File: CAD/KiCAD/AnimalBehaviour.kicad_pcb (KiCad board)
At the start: 2 copper layers, 29 parts, among them J1 Conn_01x06_Male, J10 Conn_01x02_Male, J11 Conn_01x03_Male, J12 Conn_01x02_Male, J2 Conn_01x02_Male, J3 Conn_01x04_Male, J4 Conn_01x08_Male, J5 Conn_01x02_Male, J6 Conn_01x02_Male, J7 Jack-DC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

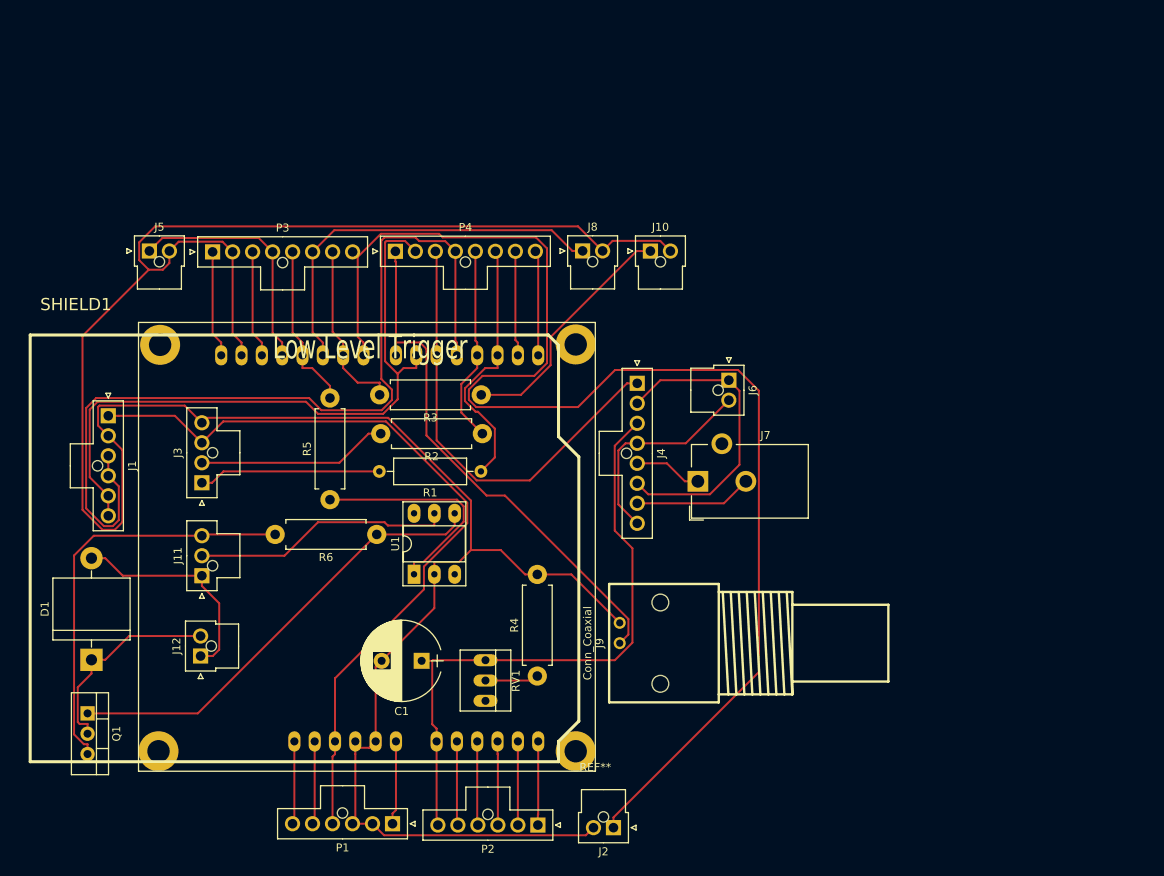
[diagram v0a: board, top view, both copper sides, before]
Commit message: Added new schematics, aduino footprints etc.
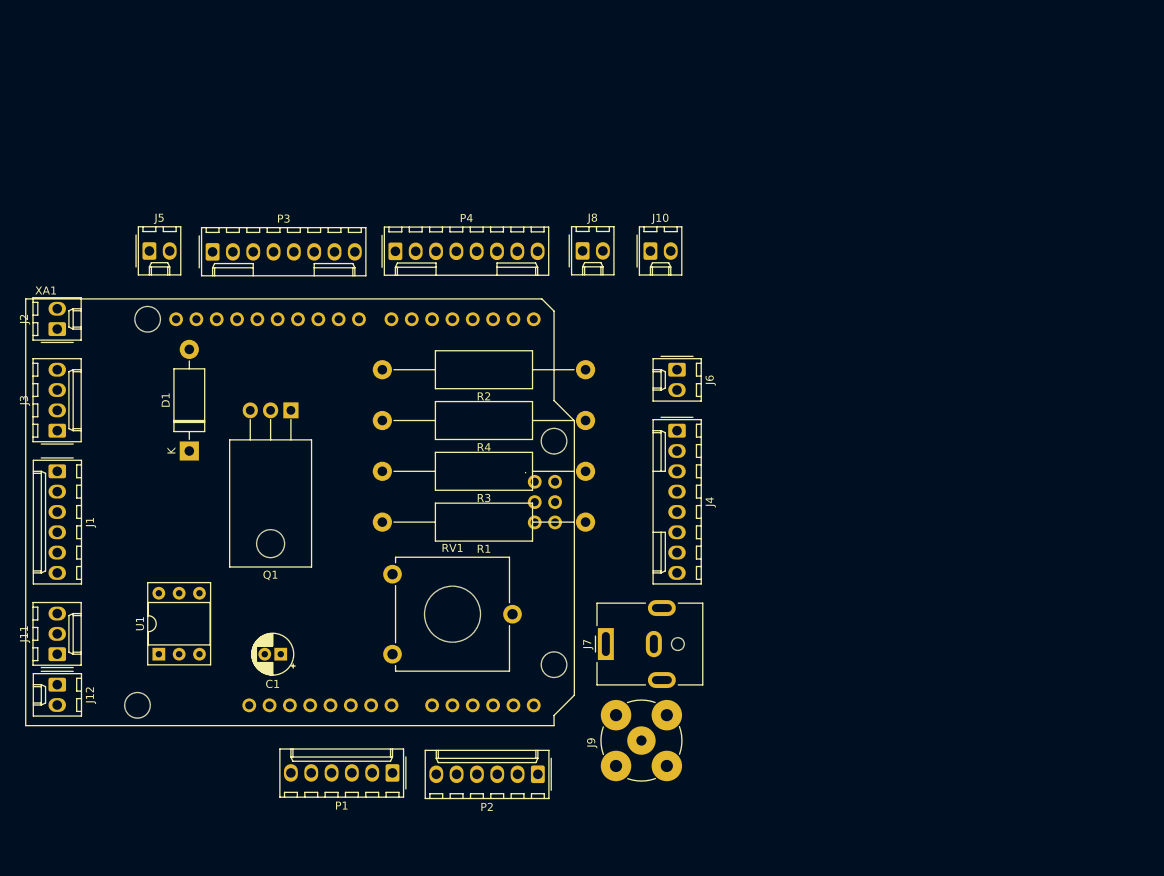
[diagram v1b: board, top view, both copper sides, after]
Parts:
- removed R5: 470E, Resistors_ThroughHole:R_Axial_DIN0411_L9.9mm_D3.6mm_P12.70mm_Horizontal
- removed R6: 10K, Resistors_ThroughHole:R_Axial_DIN0411_L9.9mm_D3.6mm_P12.70mm_Horizontal
- removed REF**: 4ChannelSSR, 4ChannelSSR
- removed SHIELD1: ARDUINO_SHIELD, arduino_shields:ARDUINO_SHIELD_040pins
- added XA1: Arduino_Uno_Shield, Arduino:Arduino_Uno_Shield, F.Cu at (86.2, 125.8)
- C1: footprint Capacitors_ThroughHole:CP_Radial_D10.0mm_P5.00mm -> Capacitor_THT:CP_Radial_D5.0mm_P2.00mm
- D1: footprint Diodes_ThroughHole:D_5KP_P12.70mm_Horizontal -> Diode_THT:D_DO-15_P12.70mm_Horizontal
- J1, P1, P2: footprint Connectors_Molex:Molex_NanoFit_1x06x2.50mm_Straight -> Connector_Molex:Molex_KK-254_AE-6410-06A_1x06_P2.54mm_Vertical
- J10, J12, J2, J5, J6, J8: footprint Connectors_Molex:Molex_NanoFit_1x02x2.50mm_Straight -> Connector_Molex:Molex_KK-254_AE-6410-02A_1x02_P2.54mm_Vertical
- J11: footprint Connectors_Molex:Molex_NanoFit_1x03x2.50mm_Straight -> Connector_Molex:Molex_KK-254_AE-6410-03A_1x03_P2.54mm_Vertical
- J3: footprint Connectors_Molex:Molex_NanoFit_1x04x2.50mm_Straight -> Connector_Molex:Molex_KK-254_AE-6410-04A_1x04_P2.54mm_Vertical
- J4, P3, P4: footprint Connectors_Molex:Molex_NanoFit_1x08x2.50mm_Straight -> Connector_Molex:Molex_KK-254_AE-6410-08A_1x08_P2.54mm_Vertical
- J7: footprint Connect:Barrel_Jack_CUI_PJ-102AH -> Connector_BarrelJack:BarrelJack_CUI_PJ-063AH_Horizontal
- J9: footprint w_conn_rf:bnc_90_1-1337543-0 -> Connector_Coaxial:BNC_TEConnectivity_1478204_Vertical
- Q1: footprint TO_SOT_Packages_THT:TO-220-3_Vertical -> Package_TO_SOT_THT:TO-220-3_Horizontal_TabDown
- R1: value 560E -> 470E; footprint Resistors_ThroughHole:R_Axial_DIN0309_L9.0mm_D3.2mm_P12.70mm_Horizontal -> Resistor_THT:R_Axial_DIN0414_L11.9mm_D4.5mm_P25.40mm_Horizontal
- R2: value 560E -> 1K; footprint Resistors_ThroughHole:R_Axial_DIN0411_L9.9mm_D3.6mm_P12.70mm_Horizontal -> Resistor_THT:R_Axial_DIN0414_L11.9mm_D4.5mm_P25.40mm_Horizontal
- R3: footprint Resistors_ThroughHole:R_Axial_DIN0411_L9.9mm_D3.6mm_P12.70mm_Horizontal -> Resistor_THT:R_Axial_DIN0414_L11.9mm_D4.5mm_P25.40mm_Horizontal
- R4: value 1K -> 10K; footprint Resistors_ThroughHole:R_Axial_DIN0411_L9.9mm_D3.6mm_P12.70mm_Horizontal -> Resistor_THT:R_Axial_DIN0414_L11.9mm_D4.5mm_P25.40mm_Horizontal
- RV1: footprint Connect:PINHEAD1-3 -> Potentiometer_THT:Potentiometer_ACP_CA14V-15_Vertical_Hole
- U1: footprint Housings_DIP:DIP-6_W7.62mm_Socket_LongPads -> Package_DIP:DIP-6_W7.62mm_Socket
- moved J2 93.4 mm to (90.2, 76.2), turned to 90 degrees
- moved Q1 45.6 mm to (119.4, 86.4), turned to 180 degrees
- moved U1 33.4 mm to (102.9, 116.8)
- moved R4 32.5 mm to (156.2, 87.6), turned to 180 degrees
- moved D1 28.8 mm to (106.7, 91.4)
- moved J7 23.4 mm to (158.8, 115.6)
- moved J11 20.6 mm to (90.2, 116.8)
- moved J3 19.2 mm to (90.2, 88.9)
- moved J12 18.3 mm to (90.2, 120.7), turned to 270 degrees
- moved C1 17.6 mm to (118.1, 116.8)
- moved R3 16.2 mm to (156.2, 94.0)
- moved J9 15.5 mm to (163.2, 127.6)
- moved R2 15.2 mm to (156.2, 81.3)
- moved R1 14.5 mm to (156.2, 100.3)
- moved RV1 11.6 mm to (132.1, 116.8), turned to 0 degrees
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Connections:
- J3 pad 1: Net-(J3-Pad1) -> D2
- J3 pad 2: Net-(J3-Pad2) -> D3
- P4 pad 7: D1 -> (no net)
- P4 pad 8: D0 -> (no net)
- R1 pad 1: D2 -> Net-(J10-Pad1)
- R1 pad 2: Net-(J3-Pad1) -> D9
- R2 pad 1: D3 -> Net-(R2-Pad1)
- R2 pad 2: Net-(J3-Pad2) -> DGND
- R3 pad 1: Net-(J10-Pad1) -> Net-(R3-Pad1)
- R3 pad 2: D9 -> D11
- R4 pad 1: Net-(R4-Pad1) -> Net-(Q1-Pad1)
- R4 pad 2: DGND -> AGND
- RV1 pad 2: Net-(R4-Pad1) -> Net-(R2-Pad1)
- RV1 pad 3: Net-(RV1-Pad3) -> (no net)
- U1 pad 1: Net-(R5-Pad1) -> Net-(R3-Pad1)
- U1 pad 3: Net-(U1-Pad3) -> (no net)
- U1 pad 6: Net-(U1-Pad6) -> (no net)
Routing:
- net DGND: track 311.3 -> 0.00 mm
- net D8: track 167.6 -> 0.00 mm
- net D4: track 110.0 -> 0.00 mm
- net 5V: track 98.7 -> 0.00 mm
- net D6: track 83.4 -> 0.00 mm
- net A0: track 77.6 -> 0.00 mm
- net D7: track 66.2 -> 0.00 mm
- net Net-(Q1-Pad1): track 57.1 -> 0.00 mm
- net D5: track 55.9 -> 0.00 mm
- net AGND: track 52.0 -> 0.00 mm
- net D10: track 49.4 -> 0.00 mm
- net PAD+: track 38.6 -> 0.00 mm
- net D2: track 32.7 -> 0.00 mm
- net EX_5V: track 32.5 -> 0.00 mm
- net Net-(J10-Pad1): track 30.7 -> 0.00 mm
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
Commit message: v2019.07.06.alpha1
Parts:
- removed the J2 at (90.2, 76.2)
- removed the J8 at (155.8, 66.4)
- removed P1, P2: CONN_6, Connector_Molex:Molex_KK-254_AE-6410-06A_1x06_P2.54mm_Vertical
- removed P3, P4: CONN_8, Connector_Molex:Molex_KK-254_AE-6410-08A_1x08_P2.54mm_Vertical
- removed the R2 at (156.2, 81.3)
- removed the R4 at (156.2, 87.6)
- added Assr4ch1: PCB_SSR_4Ch_LLT, SSR4Channel:4ChannelSSR, F.Cu at (169.5, 95.0)
- added J11: Imaging, BhallaLab:Connector_Mini-DIN_Female_6Pin_2rows, F.Cu at (140.5, 48.0)
- added J13: StimIsoIN, Connector_Molex:Molex_KK-254_AE-6410-02A_1x02_P2.54mm_Vertical, F.Cu at (213.0, 53.0)
- added J4: StimIsoIN, Connector_Coaxial:BNC_TEConnectivity_1478204_Vertical, F.Cu at (204.3, 51.3)
- added R1: 1K, Resistor_THT:R_Axial_DIN0414_L11.9mm_D4.5mm_P25.40mm_Horizontal, F.Cu at (166.8, 72.8)
- added R3: 10K, Resistor_THT:R_Axial_DIN0414_L11.9mm_D4.5mm_P25.40mm_Horizontal, F.Cu at (173.1, 72.8)
- added RotaryEncoder1: Orange Optical RotaryEncoder, Connector_Molex:Molex_KK-254_AE-6410-04A_1x04_P2.54mm_Vertical, F.Cu at (135.5, 95.0)
- added ShockPad1: ShockPad, TerminalBlock:TerminalBlock_Altech_AK300-2_P5.00mm, F.Cu at (216.0, 95.5)
- J1: value Conn_01x06_Male -> SSR_INPUT; footprint Connector_Molex:Molex_KK-254_AE-6410-06A_1x06_P2.54mm_Vertical -> Connector_Molex:Molex_KK-254_AE-6410-04A_1x04_P2.54mm_Vertical
- J10: value Conn_01x02_Male -> Cam; footprint Connector_Molex:Molex_KK-254_AE-6410-02A_1x02_P2.54mm_Vertical -> BhallaLab:Connector_Mini-DIN_Female_6Pin_2rows
- J2: renamed from J4; value Conn_01x08_Male -> SSR OUT
- J3: value Conn_01x04_Male -> StimCurrentInject; footprint Connector_Molex:Molex_KK-254_AE-6410-04A_1x04_P2.54mm_Vertical -> Connector_BarrelJack:BarrelJack_CUI_PJ-063AH_Horizontal
- J5: value Conn_01x02_Male -> ImagingTrig
- J6: value Conn_01x02_Male -> CAM
- J7: value Jack-DC -> AudioJack2; footprint Connector_BarrelJack:BarrelJack_CUI_PJ-063AH_Horizontal -> Connector_Audio:Jack_3.5mm_CUI_SJ-3523-SMT_Horizontal
- J9: value Conn_Coaxial -> LED; footprint Connector_Coaxial:BNC_TEConnectivity_1478204_Vertical -> Connector_Molex:Molex_KK-254_AE-6410-02A_1x02_P2.54mm_Vertical
- RV1: footprint Potentiometer_THT:Potentiometer_ACP_CA14V-15_Vertical_Hole -> Potentiometer_THT:Potentiometer_Alps_RK09L_Single_Vertical
- moved J3 121.2 mm to (210.0, 107.0)
- moved RV1 81.3 mm to (200.5, 73.0)
- moved U1 78.1 mm to (180.5, 108.0), turned to 180 degrees
- moved J9 76.0 mm to (182.0, 54.0), turned to 0 degrees
- moved J7 75.5 mm to (192.5, 48.0), turned to 0 degrees
- moved C1 70.2 mm to (187.5, 106.0)
- moved J2 56.0 mm to (218.0, 64.5)
- moved D1 55.0 mm to (158.5, 73.0), turned to 270 degrees
- moved J5 50.6 mm to (150.5, 53.0)
- moved J1 46.6 mm to (135.5, 83.0), turned to 90 degrees
- moved J8 45.8 mm to (134.7, 105.8)
- moved XA1 45.8 mm to (130.7, 114.8)
- moved J12 45.0 mm to (134.5, 113.0), turned to 90 degrees
- moved R4 40.4 mm to (185.8, 72.8), turned to 270 degrees
- moved Q1 40.3 mm to (159.5, 90.0)
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- renumbered J11 to J8, R3 to R2, R1 to R4
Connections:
- net D11 renamed Puff
- net D12 renamed ImagingTrig
- net D9 renamed LED
- C1 pad 1: A0 -> ShockRead
- J1 pad 3: D4 -> ShockRelayCh12
- J1 pad 4: D4 -> ShockRelayCh34
- J10 pad 1: Net-(J10-Pad1) -> (no net)
- J10 pad 2: DGND -> CamTTL
- J2 pad 1: D5 -> PAD-
- J2 pad 2: PAD+ -> OUT-
- J2 pad 3: A0 -> PAD+
- J2 pad 4: PAD- -> OUT+
- J2 pad 5: OUT+ -> PAD-
- J2 pad 6: PAD+ -> ShockRead
- J2 pad 7: OUT- -> PAD+
- J2 pad 8: PAD- -> ShockPWM
- J3 pad 1: D2 -> OUT+
- J3 pad 2: D3 -> OUT-
- J6 pad 1: PAD+ -> CamTTL
- J6 pad 2: PAD- -> DGND
- J9 pad 1: D7 -> Net-(J9-Pad1)
- R4 pad 1: Net-(J10-Pad1) -> Net-(J9-Pad1)
- RV1 pad 1: A0 -> ShockRead
- XA1 pad 3V3: 3V3 -> (no net)
- XA1 pad A0: A0 -> ShockRead
- XA1 pad A1: A1 -> (no net)
- XA1 pad A2: A2 -> (no net)
- XA1 pad A3: A3 -> (no net)
- XA1 pad A4: A4 -> (no net)
- XA1 pad A5: A5 -> (no net)
- XA1 pad AREF: AREF -> (no net)
- XA1 pad D10: D10 -> CamTTL
- XA1 pad D13: D13 -> (no net)
- XA1 pad D2: D2 -> EncA
- XA1 pad D3: D3 -> EncB
- XA1 pad D4: D4 -> ShockRelayCh12
- XA1 pad D5: D5 -> ShockPWM
- XA1 pad D6: D6 -> ShockRelayCh34
- XA1 pad D7: D7 -> ShockStimIsolator
- XA1 pad D8: D8 -> TONE+
- XA1 pad RST1: RST -> (no net)
- XA1 pad VIN: V_IN -> (no net)

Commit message: Got a PCB layout.
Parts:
- moved J7 24.4 mm to (209.0, 66.0), turned to 90 degrees
- moved J2 9.51 mm to (218.5, 74.0)
- moved J3 9.51 mm to (210.5, 116.5)
- moved RV1 9.51 mm to (201.0, 82.5)
- moved ShockPad1 9.51 mm to (216.5, 105.0)
- moved J13 6.08 mm to (207.0, 54.0)
- moved J4 6.08 mm to (198.3, 52.3)
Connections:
- C1 pad 2: DGND -> AGND
- J1 pad 2: DGND -> AGND
- J10 pad 6: DGND -> AGND
- J11 pad 6: DGND -> AGND
- J13 pad 1: DGND -> AGND
- J4 pad 2: DGND -> AGND
- J5 pad 2: DGND -> AGND
- J6 pad 2: DGND -> AGND
- J9 pad 2: DGND -> AGND
- R1 pad 2: DGND -> AGND
- RotaryEncoder1 pad 4: DGND -> AGND
- U1 pad 2: DGND -> AGND
- XA1 pad GND1: DGND -> AGND

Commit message: Archives and other updates.
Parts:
- moved R1 30.7 mm to (187.7, 95.2), turned to 90 degrees
- moved R4 28.2 mm to (168.7, 95.2), turned to 90 degrees
- moved R3 23.9 mm to (181.4, 95.2), turned to 90 degrees
- moved R2 22.9 mm to (175.0, 95.2), turned to 90 degrees
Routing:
- net AGND: track 0.00 -> 372.3 mm
- net PAD-: track 0.00 -> 96.2 mm
- net 5V: track 0.00 -> 74.1 mm
- net ShockPWM: track 0.00 -> 69.8 mm
- net TONE+: track 0.00 -> 69.3 mm
- net EncA: track 0.00 -> 69.2 mm
- net EncB: track 0.00 -> 65.2 mm
- net ShockRead: track 0.00 -> 65.0 mm
- net ShockRelayCh12: track 0.00 -> 56.2 mm
- net ShockStimIsolator: track 0.00 -> 56.2 mm
- net EX_5V: track 0.00 -> 55.8 mm
- net Net-(D1-Pad1): track 0.00 -> 55.7 mm
- net Net-(J9-Pad1): track 0.00 -> 53.6 mm
- net ShockRelayCh34: track 0.00 -> 52.0 mm
- net OUT-: track 0.00 -> 44.1 mm
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
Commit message: Tag this version and release.
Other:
- board outline added: 104 x 83 mm
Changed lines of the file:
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@@
   (general
     (thickness 1.6)
-    (drawings 0)
+    (drawings 5)
     (tracks 314)
     (zones 0)
@@
       (usegerberattributes false)
       (usegerberadvancedattributes false)
-      (creategerberjobfile false)
+      (creategerberjobfile true)
       (excludeedgelayer true)
-      (linewidth 0.100000)
-      (plotframeref false)
+      (linewidth 0.200000)
+      (plotframeref true)
       (viasonmask false)
       (mode 1)
@@
       (outputformat 1)
       (mirror false)
-      (drillshape 1)
+      (drillshape 0)
       (scaleselection 1)
-      (outputdirectory ""))
+      (outputdirectory "GERBER/"))
   )
   (net 0 "")
@@
     )
   )
+  (gr_line (start 122.5 123.5) (end 122.5 40.5) (layer Edge.Cuts) (width 0.1))
+  (gr_line (start 226.5 123.5) (end 122.5 123.5) (layer Edge.Cuts) (width 0.1))
+  (gr_line (start 226.5 59) (end 226.5 123.5) (layer Edge.Cuts) (width 0.1))
+  (gr_line (start 208 40.5) (end 226.5 59) (layer Edge.Cuts) (width 0.1))
+  (gr_line (start 122.5 40.5) (end 208 40.5) (layer Edge.Cuts) (width 0.1))
   (segment (start 134.67 105.84) (end 154.81 85.7) (width 0.25) (layer F.Cu) (net 1))
   (segment (start 154.81 85.7) (end 158.5 85.7) (width 0.25) (layer F.Cu) (net 1))
